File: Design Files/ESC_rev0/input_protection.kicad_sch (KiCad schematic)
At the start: 13 parts, among them U1 XT30PW-M, U2 XH-2PWBPZ

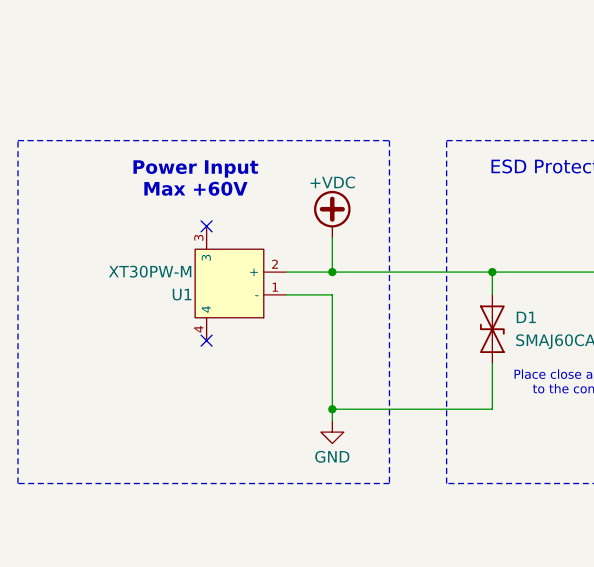
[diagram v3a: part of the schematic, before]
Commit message: update 15
Simple connectors replaced by smd connectors (downloaded). Connectors were placed in edges of the board.
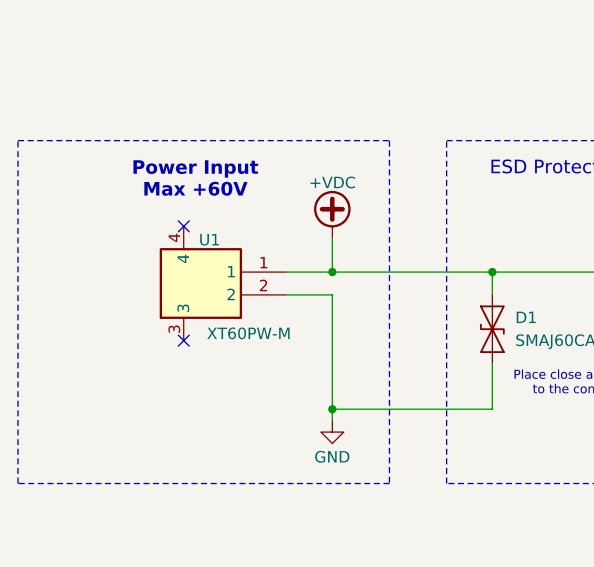
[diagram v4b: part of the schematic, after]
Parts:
- U1: value XT30PW-M -> XT60PW-M; footprint Connector_AMASS:AMASS_XT30PW-M_1x02_P2.50mm_Horizontal -> XT60PWM; symbol XT30PW-M:XT30PW-M -> XT60PW-M:XT60PW-M; Height (none) -> 8.4; Manufacturer_Name (none) -> Changzou Amass Elec; Manufacturer_Part_Number (none) -> XT60PW-M
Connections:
- net +VDC: now also U1.1; no longer U1.2 (+)
- net GND: now also U1.2; no longer U1.1 (-)
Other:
- moved on the sheet: U1
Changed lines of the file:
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@@
 	)
 	(no_connect
-		(at 49.53 72.39)
+		(at 46.99 72.39)
 	)
 	(no_connect
-		(at 49.53 85.09)
+		(at 46.99 85.09)
 	)
 	(wire
@@
 	)
 	(symbol
-		(lib_id "XT30PW-M:XT30PW-M")
-		(at 53.34 78.74 270)
+		(lib_id "XT60PW-M:XT60PW-M")
+		(at 49.53 78.74 0)
 		(mirror x)
 		(unit 1)
@@
 		(dnp no)
 		(property "Reference" "U1"
-			(at 48.006 80.01 90)
+			(at 51.054 73.914 0)
 			(effects
 				(font
@@
 			)
 		)
-		(property "Value" "XT30PW-M"
-			(at 48.006 77.47 90)
+		(property "Value" "XT60PW-M"
+			(at 58.928 84.328 0)
 			(effects
 				(font
@@
 			)
 		)
-		(property "Footprint" "Connector_AMASS:AMASS_XT30PW-M_1x02_P2.50mm_Horizontal"
-			(at 43.18 78.74 0)
-			(effects
-				(font
-					(size 1.27 1.27)
-					(italic yes)
-				)
-				(hide yes)
-			)
-		)
-		(property "Datasheet" "https://cn.bing.com/search?q=datasheet: XT30PW-M"
-			(at 53.467 81.026 0)
-			(effects
-				(font
-					(size 1.27 1.27)
-				)
-				(justify left)
-				(hide yes)
-			)
-		)
-		(property "Description" ""
-			(at 53.34 78.74 0)
+		(property "Footprint" "XT60PWM"
+			(at 66.04 -16.18 0)
+			(effects
+				(font
+					(size 1.27 1.27)
+				)
+				(justify left top)
+				(hide yes)
+			)
+		)
+		(property "Datasheet" "https://www.tme.eu/Document/9b8d0c5eb7094295f3d3112c214d3ade/XT60PW%20SPEC.pdf"
+			(at 66.04 -116.18 0)
+			(effects
+				(font
+					(size 1.27 1.27)
+				)
+				(justify left top)
+				(hide yes)
+			)
+		)
+		(property "Description" "Socket; DC supply; XT60; male; PIN: 2; on PCBs; THT; Colour: yellow"
+			(at 58.928 64.262 0)
 			(effects
 				(font
@@
 		)
 		(property "LCSC" "C431092"
-			(at 53.34 78.74 0)
-			(effects
-				(font
-					(size 1.27 1.27)
-				)
-				(hide yes)
-			)
+			(at 49.53 78.74 0)
+			(effects
+				(font
+					(size 1.27 1.27)
+				)
+				(hide yes)
+			)
+		)
+		(property "Height" "8.4"
+			(at 66.04 -316.18 0)
+			(effects
+				(font
+					(size 1.27 1.27)
+				)
+				(justify left top)
+				(hide yes)
+			)
+		)
+		(property "Manufacturer_Name" "Changzou Amass Elec"
+			(at 66.04 -416.18 0)
+			(effects
+				(font
+					(size 1.27 1.27)
+				)
+				(justify left top)
+				(hide yes)
+			)
+		)
+		(property "Manufacturer_Part_Number" "XT60PW-M"
+			(at 66.04 -516.18 0)
+			(effects
+				(font
+					(size 1.27 1.27)
+				)
+				(justify left top)
+				(hide yes)
+			)
+		)
+		(property "Mouser Part Number" ""
+			(at 66.04 -616.18 0)
+			(effects
+				(font
+					(size 1.27 1.27)
+				)
+				(justify left top)
+				(hide yes)
+			)
+		)
+		(property "Mouser Price/Stock" ""
+			(at 66.04 -716.18 0)
+			(effects
+				(font
+					(size 1.27 1.27)
+				)
+				(justify left top)
+				(hide yes)
+			)
+		)
+		(property "Arrow Part Number" ""
+			(at 66.04 -816.18 0)
+			(effects
+				(font
+					(size 1.27 1.27)
+				)
+				(justify left top)
+				(hide yes)
+			)
+		)
+		(property "Arrow Price/Stock" ""
+			(at 66.04 -916.18 0)
+			(effects
+				(font
+					(size 1.27 1.27)
+				)
+				(justify left top)
+				(hide yes)
+			)

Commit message: update 16
All components placed on board. Some components modifications and addition were made: added 3D models, changed some symbols and footprints positions and some component types.
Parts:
- C3, C4: footprint Capacitor_SMD:C_0201_0603Metric -> Capacitor_SMD:C_0603_1608Metric
- D2: footprint LED_SMD:LED_0201_0603Metric -> LED_SMD:LED_0805_2012Metric
- TH1: footprint Capacitor_THT:C_Radial_D4.0mm_H5.0mm_P1.50mm -> Capacitor_SMD:C_0603_1608Metric_Pad1.08x0.95mm_HandSolder
- U1: footprint XT60PWM -> XT60PW-M:XT60PWM
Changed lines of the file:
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@@
 			)
 		)
-		(property "Footprint" "Capacitor_SMD:C_0201_0603Metric"
+		(property "Footprint" "Capacitor_SMD:C_0603_1608Metric"
 			(at 180.0352 97.79 0)
 			(effects
@@
 			)
 		)
-		(property "Footprint" "XT60PWM"
+		(property "Footprint" "XT60PW-M:XT60PWM"
 			(at 66.04 -16.18 0)
 			(effects
@@
 			)
 		)
-		(property "Footprint" "Capacitor_THT:C_Radial_D4.0mm_H5.0mm_P1.50mm"
+		(property "Footprint" "Capacitor_SMD:C_0603_1608Metric_Pad1.08x0.95mm_HandSolder"
 			(at 133.35 144.78 0)
 			(effects
@@
 			)
 		)
-		(property "Footprint" "LED_SMD:LED_0201_0603Metric"
+		(property "Footprint" "LED_SMD:LED_0805_2012Metric"
 			(at 212.09 92.71 0)
 			(effects
@@
 			)
 		)
-		(property "Footprint" "Capacitor_SMD:C_0201_0603Metric"
+		(property "Footprint" "Capacitor_SMD:C_0603_1608Metric"
 			(at 147.0152 129.54 0)
 			(effects

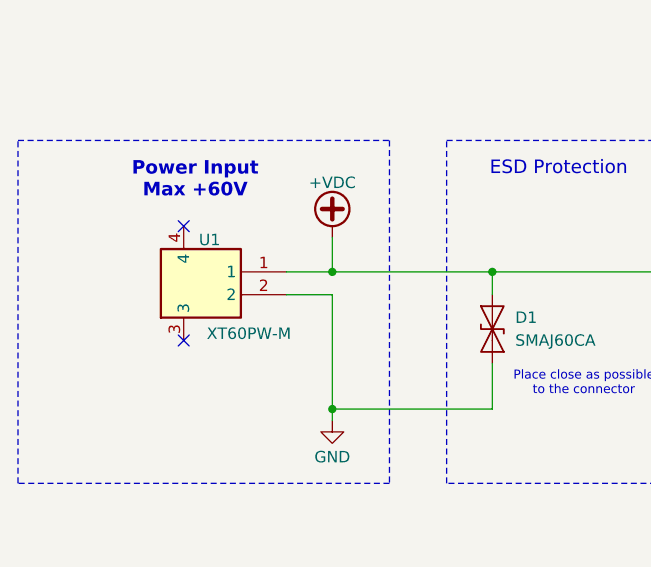
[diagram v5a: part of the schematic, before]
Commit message: update 18
Route process partially complete. Some corrections were made in footprints and pins references. Probably the power lines will need changes in size.
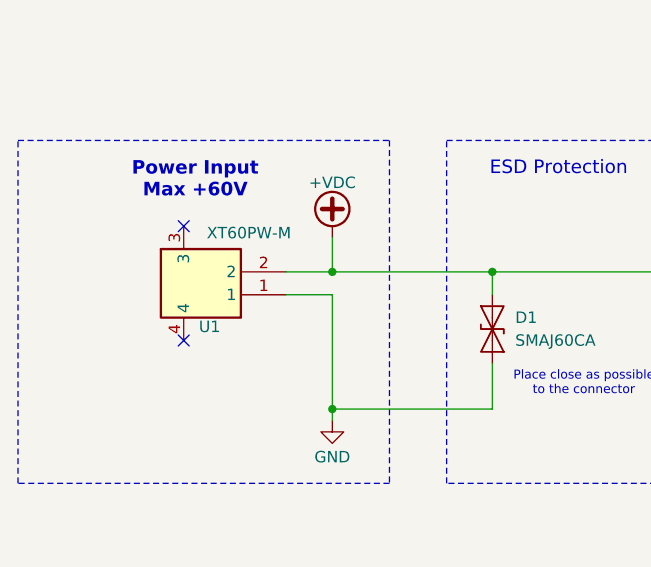
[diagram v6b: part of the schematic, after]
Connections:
- net +VDC: now also U1.2; no longer U1.1
- net GND: now also U1.1; no longer U1.2
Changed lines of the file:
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@@
+	)
+	(junction
+		(at 63.5 77.47)
+		(diameter 0)
+		(color 0 0 0 0)
 	)
 	(junction
@@
 	)
 	(junction
-		(at 63.5 77.47)
-		(diameter 0)
-		(color 0 0 0 0)
-	)
-	(junction
 		(at 212.09 77.47)
 		(diameter 0)
@@
 	(wire
 		(pts
-			(xy 63.5 80.01) (xy 58.42 80.01)
-		)
-		(stroke
-			(width 0)
-			(type default)
-		)
-	)
-	(wire
-		(pts
 			(xy 133.35 149.86) (xy 133.35 152.4)
 		)
@@
 	(wire
 		(pts
+			(xy 58.42 77.47) (xy 63.5 77.47)
+		)
+		(stroke
+			(width 0)
+			(type default)
+		)
+	)
+	(wire
+		(pts
 			(xy 63.5 77.47) (xy 63.5 73.66)
 		)
@@
 	(wire
 		(pts
-			(xy 58.42 77.47) (xy 63.5 77.47)
-		)
-		(stroke
-			(width 0)
-			(type default)
-		)
-	)
-	(wire
-		(pts
 			(xy 128.27 77.47) (xy 128.27 80.01)
 		)
@@
 		(pts
 			(xy 133.35 139.7) (xy 140.97 139.7)
+		)
+		(stroke
+			(width 0)
+			(type default)
+		)
+	)
+	(wire
+		(pts
+			(xy 58.42 80.01) (xy 63.5 80.01)
 		)
 		(stroke
@@
 		(lib_id "XT60PW-M:XT60PW-M")
 		(at 49.53 78.74 0)
-		(mirror x)
 		(unit 1)
 		(exclude_from_sim no)
@@
 		(dnp no)
 		(property "Reference" "U1"
-			(at 51.054 73.914 0)
+			(at 51.054 83.566 0)
 			(effects
 				(font
@@
 		)
 		(property "Value" "XT60PW-M"
-			(at 58.928 84.328 0)
+			(at 58.928 73.152 0)
 			(effects
 				(font
@@
 		)
 		(property "Footprint" "XT60PW-M:XT60PWM"
-			(at 66.04 -16.18 0)
+			(at 66.04 173.66 0)
 			(effects
 				(font
@@
 		)
 		(property "Datasheet" "https://www.tme.eu/Document/9b8d0c5eb7094295f3d3112c214d3ade/XT60PW%20SPEC.pdf"
-			(at 66.04 -116.18 0)
+			(at 66.04 273.66 0)
 			(effects
 				(font
@@
 		)
 		(property "Description" "Socket; DC supply; XT60; male; PIN: 2; on PCBs; THT; Colour: yellow"
-			(at 58.928 64.262 0)
+			(at 58.928 93.218 0)
 			(effects
 				(font
@@
 		)
 		(property "Height" "8.4"
-			(at 66.04 -316.18 0)
+			(at 66.04 473.66 0)
 			(effects
 				(font
@@
 		)
 		(property "Manufacturer_Name" "Changzou Amass Elec"
-			(at 66.04 -416.18 0)
+			(at 66.04 573.66 0)
 			(effects
 				(font
@@
 		)
 		(property "Manufacturer_Part_Number" "XT60PW-M"
-			(at 66.04 -516.18 0)
+			(at 66.04 673.66 0)
 			(effects
 				(font
@@
 		)
 		(property "Mouser Part Number" ""
-			(at 66.04 -616.18 0)
+			(at 66.04 773.66 0)
 			(effects
 				(font
@@
 		)
 		(property "Mouser Price/Stock" ""
-			(at 66.04 -716.18 0)
+			(at 66.04 873.66 0)
 			(effects
 				(font
@@
 		)
 		(property "Arrow Part Number" ""
-			(at 66.04 -816.18 0)
+			(at 66.04 973.66 0)
 			(effects
 				(font
@@
 		)
 		(property "Arrow Price/Stock" ""
-			(at 66.04 -916.18 0)
-			(effects
-				(font
+			(at 66.04 1073.66 0)
+			(effects
+				(font
